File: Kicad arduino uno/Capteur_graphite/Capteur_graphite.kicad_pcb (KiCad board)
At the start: 2 copper layers, 68.6 x 53.3 mm, 25 parts, among them J1 Power, J2 Digital/PWM, J3 Analog, J4 Digital/PWM, U3 MCP41050, U4 LTC1050

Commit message: masse flottante à refaire
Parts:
- moved U3 31.6 mm to (112.4, 51.9)
- moved R5 2.00 mm to (148.4, 93.5)
- moved U7 2.00 mm to (164.5, 92.0)
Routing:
- net P13: track 68.2 -> 28.5 mm
- net Net-(U3-PB0): track 62.2 -> 32.7 mm
- net P11: track 52.9 -> 34.1 mm
- net P10: track 48.6 -> 35.4 mm
- net +5V: track 193.8 -> 205.7 mm
- net A0: track 13.3 -> 11.3 mm
- net Net-(C4-Pad1): track 25.4 -> 24.2 mm
- net Net-(U5-OUT): track 6.21 -> 5.62 mm
- net P2: track 23.3 -> 22.7 mm

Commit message: Save_avec_via
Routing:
- net GND: track 0.00 -> 19.4 mm, vias 0 -> 6
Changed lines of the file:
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@@
+	)
+	(segment
+		(start 119.5 96.5)
+		(end 124 92)
+		(width 0.5)
+		(layer "F.Cu")
+		(net 1)
+	)
+	(segment
+		(start 135 92)
+		(end 141 92)
+		(width 0.5)
+		(layer "F.Cu")
+		(net 1)
+	)
+	(segment
+		(start 131.5 57.5)
+		(end 138.5 57.5)
+		(width 0.5)
+		(layer "F.Cu")
+		(net 1)
+	)
+	(via
+		(at 131.5 57.5)
+		(size 2)
+		(drill 1)
+		(layers "F.Cu" "B.Cu")
+		(free yes)
+		(net 1)
+	)
+	(via
+		(at 124 92)
+		(size 2)
+		(drill 1)
+		(layers "F.Cu" "B.Cu")
+		(free yes)
+		(net 1)
+	)
+	(via
+		(at 135 92)
+		(size 2)
+		(drill 1)
+		(layers "F.Cu" "B.Cu")
+		(free yes)
+		(net 1)
+	)
+	(via
+		(at 138.5 57.5)
+		(size 2)
+		(drill 1)
+		(layers "F.Cu" "B.Cu")
+		(free yes)
+		(net 1)
+	)
+	(via
+		(at 141 92)
+		(size 2)
+		(drill 1)
+		(layers "F.Cu" "B.Cu")
+		(free yes)
+		(net 1)
+	)
+	(via
+		(at 119.5 96.5)
+		(size 2)
+		(drill 1)
+		(layers "F.Cu" "B.Cu")
+		(free yes)
+		(net 1)
 	)
 	(segment

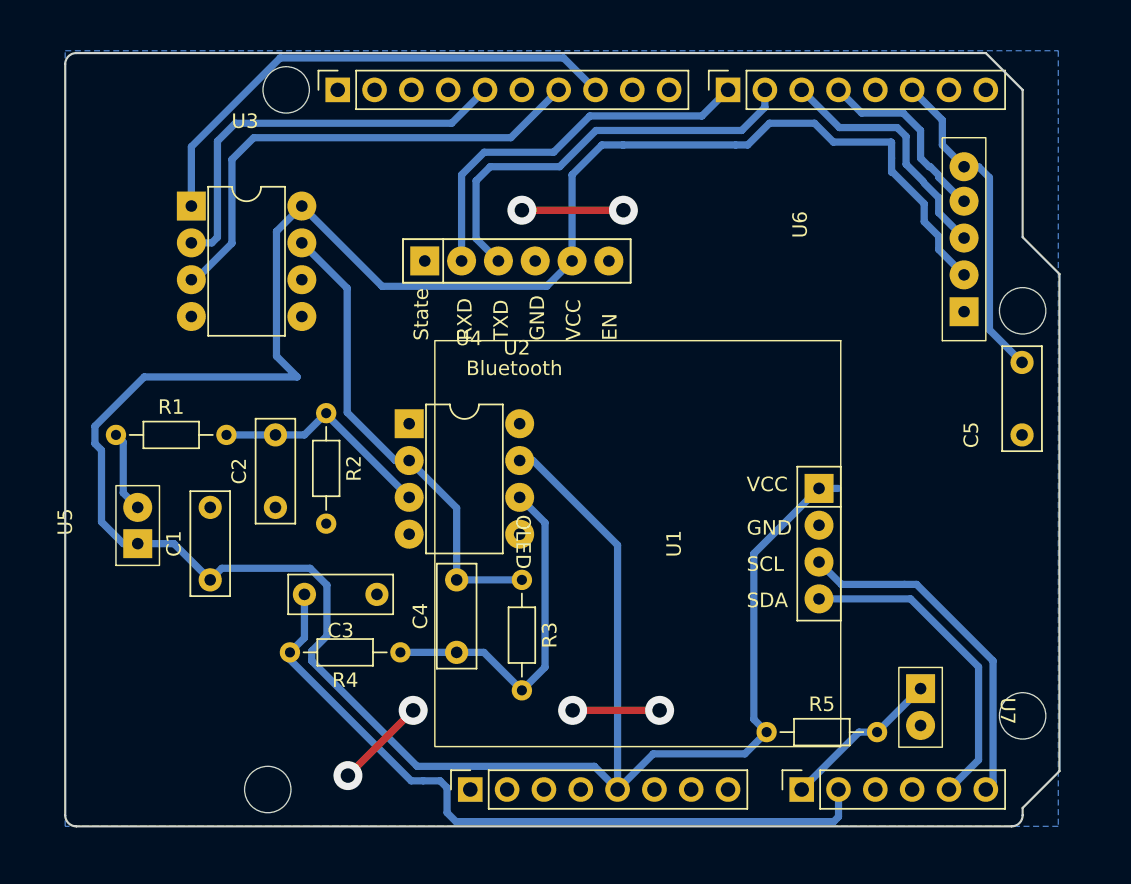
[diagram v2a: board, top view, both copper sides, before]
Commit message: Save_sans_via_mais_avec_modif_pin
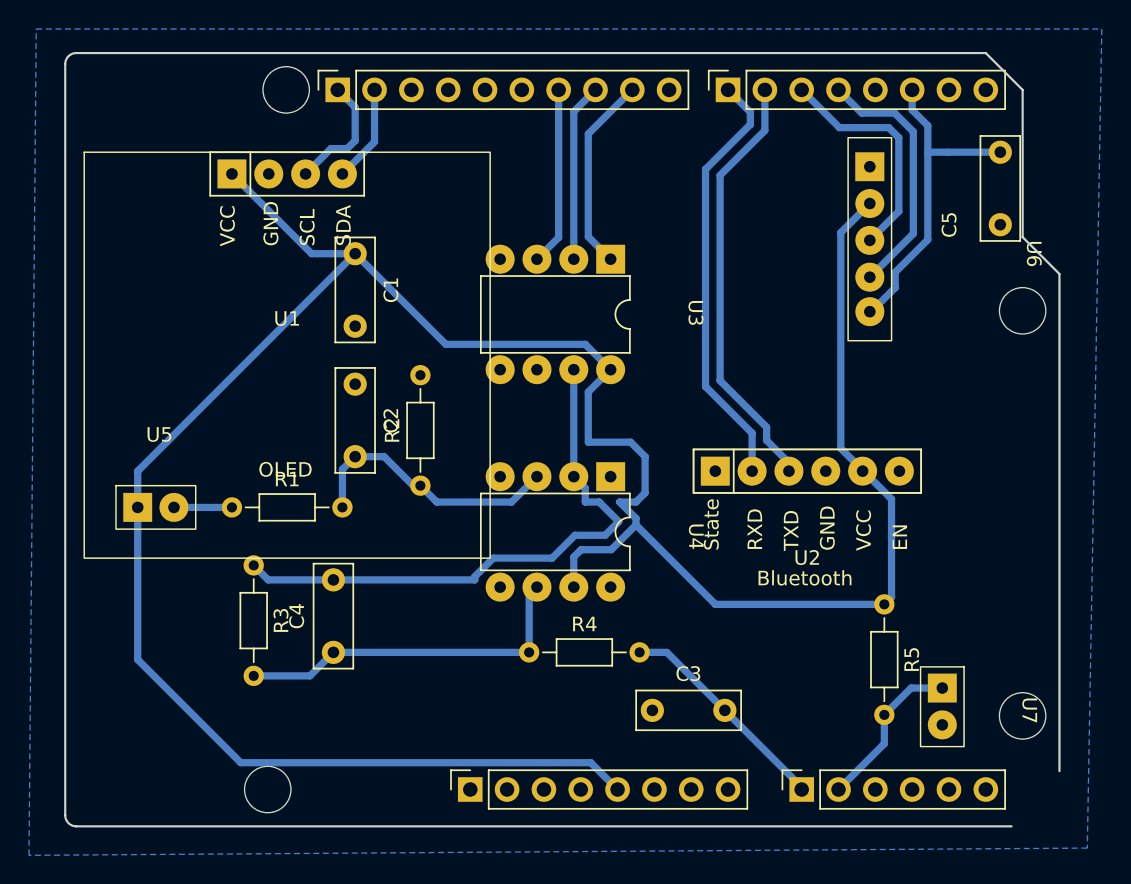
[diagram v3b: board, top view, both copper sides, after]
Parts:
- moved U1 44.7 mm to (115.3, 55.0), turned to 0 degrees
- moved U3 33.1 mm to (143.0, 64.6), turned to -90 degrees
- moved U2 24.7 mm to (151.2, 75.5)
- moved C1 24.6 mm to (120.0, 60.5), turned to -90 degrees
- moved C3 20.6 mm to (140.5, 92.0), turned to 0 degrees
- moved U4 20.1 mm to (143.0, 80.0), turned to -90 degrees
- moved R3 18.5 mm to (113.0, 82.0)
- moved C5 14.6 mm to (164.5, 58.5)
- moved R5 12.0 mm to (156.5, 84.7), turned to -90 degrees
- moved C2 10.1 mm to (120.0, 69.5), turned to -90 degrees
- moved R1 9.43 mm to (111.5, 78.0)
- moved R4 8.88 mm to (132.0, 88.0), turned to 0 degrees
- moved C4 8.50 mm to (118.5, 88.0)
- moved R2 8.20 mm to (124.5, 76.5), turned to 90 degrees
- moved U5 8.14 mm to (106.5, 73.5), turned to 0 degrees
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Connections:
- C3 pad 2: A1 -> A0
- J2 pad 5: P13 -> /13
- J2 pad 9: /*9 -> P9
- R4 pad 2: A1 -> A0
- R5 pad 2: A0 -> A1
- U3 pad 1: P10 -> P9
- U3 pad 2: P13 -> P10
- U7 pad 1: A0 -> A1
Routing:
- net A1: track 50.4 -> 11.2 mm
- net +5V: track 205.7 -> 176.6 mm
- net P13: track 28.5 -> 0.00 mm
- net P10: track 35.4 -> 12.3 mm
- net P11: track 34.1 -> 12.3 mm
- net GND: track 19.4 -> 0.00 mm, vias 6 -> 0
- net A4: track 22.3 -> 6.72 mm
- net A5: track 23.9 -> 8.37 mm
- net P9: track 0.00 -> 13.6 mm
- net Net-(U3-PB0): track 32.7 -> 39.7 mm
- net P4: track 13.0 -> 17.6 mm
- net A0: track 11.3 -> 15.2 mm
- net P7: track 26.7 -> 29.5 mm
- net Net-(C2-Pad2): track 15.7 -> 18.4 mm
- net Net-(U5-OUT): track 5.62 -> 4.00 mm
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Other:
- outline, holes or cut-outs redrawn
- board text removed: "${REFERENCE}"
- board text removed: "ICSP"

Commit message: sans_via_mais_bonne_modif_pin_(SCK_sur_la_13)
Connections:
- J2 pad 5: /13 -> P13
- J2 pad 8: P10 -> /*10
- U3 pad 2: P10 -> P13
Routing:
- net P13: track 0.00 -> 39.2 mm
- net P10: track 12.3 -> 0.00 mm
- net P11: track 12.3 -> 18.7 mm
- net P2: track 22.5 -> 24.0 mm
- net P9: track 13.6 -> 12.3 mm
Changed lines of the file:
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@@
 	(net 7 "/12")
 	(net 8 "/AREF")
-	(net 9 "/13")
+	(net 9 "P13")
 	(net 10 "/TX{slash}1")
 	(net 11 "/*3")
@@
 	(net 19 "unconnected-(U2-State-Pad1)")
 	(net 20 "unconnected-(U2-EN-Pad6)")
-	(net 21 "P10")
+	(net 21 "/*10")
 	(net 22 "P11")
 	(net 23 "Net-(U5-OUT)")
@@
 			(layers "*.Cu" "*.Mask")
 			(remove_unused_layers no)
-			(net 9 "/13")
+			(net 9 "P13")
 			(pinfunction "Pin_5")
 			(pintype "passive")
@@
 			(layers "*.Cu" "*.Mask")
 			(remove_unused_layers no)
-			(net 21 "P10")
+			(net 21 "/*10")
 			(pinfunction "Pin_8")
 			(pintype "passive")
@@
 		(tags "C Disc series Radial pin pitch 5.00mm  diameter 7mm width 2.5mm Capacitor")
 		(property "Reference" "C3"
-			(at 2.5 -2.5 360)
+			(at 2.5 -2.5 0)
 			(layer "F.SilkS")
 			(effects
@@
 		)
 		(property "Value" "C"
-			(at 2.5 2.5 360)
+			(at 2.5 2.5 0)
 			(layer "F.Fab")
 			(effects
@@
 		)
 		(fp_text user "${REFERENCE}"
-			(at 2.5 0 360)
+			(at 2.5 0 0)
 			(layer "F.Fab")
 			(effects
@@
 			(layers "*.Cu" "*.Mask")
 			(remove_unused_layers no)
-			(net 21 "P10")
+			(net 9 "P13")
 			(pinfunction "SCK")
 			(pintype "passive")
@@
 		(tags "Resistor Axial_DIN0204 series Axial Horizontal pin pitch 7.62mm 0.167W length 3.6mm diameter 1.6mm")
 		(property "Reference" "R4"
-			(at 3.81 -1.92 360)
+			(at 3.81 -1.92 0)
 			(layer "F.SilkS")
 			(effects
@@
 		)
 		(property "Value" "R"
-			(at 3.81 1.92 360)
+			(at 3.81 1.92 0)
 			(layer "F.Fab")
 			(effects
@@
 		)
 		(fp_text user "${REFERENCE}"
-			(at 3.81 0 360)
+			(at 3.81 0 0)
 			(layer "F.Fab")
 			(effects
@@
 		(at 115.31 55)
 		(property "Reference" "U1"
-			(at 0 10 360)
+			(at 0 10 0)
 			(layer "F.SilkS")
 			(effects
@@
 		)
 		(property "Value" "~"
-			(at 0 -2.5 360)
+			(at 0 -2.5 0)
 			(layer "F.Fab")
 			(effects
@@
 		)
 		(property "Footprint" "Librairie_d_empreinte:OLED"
-			(at 0 0 360)
+			(at 0 0 0)
 			(layer "F.Fab")
 			(hide yes)
@@
 		)
 		(property "Datasheet" ""
-			(at 0 0 360)
+			(at 0 0 0)
 			(layer "F.Fab")
 			(hide yes)
@@
 		)
 		(property "Description" ""
-			(at 0 0 360)
+			(at 0 0 0)
 			(layer "F.Fab")
 			(hide yes)
@@
 		(tags "Resistor Axial_DIN0204 series Axial Horizontal pin pitch 7.62mm 0.167W length 3.6mm diameter 1.6mm")
 		(property "Reference" "R1"
-			(at 3.81 -1.92 360)
+			(at 3.81 -1.92 0)
 			(layer "F.SilkS")
 			(effects
@@
 		)
 		(property "Value" "R"
-			(at 3.81 1.92 360)
+			(at 3.81 1.92 0)
 			(layer "F.Fab")
 			(effects
@@
 		)
 		(fp_text user "${REFERENCE}"
-			(at 3.81 0 360)
+			(at 3.81 0 0)
 			(layer "F.Fab")
 			(effects
@@
 		(layer "Edge.Cuts")
 	)
+	(gr_line
+		(start 168.58 96.19)
+		(end 165.278 100)
+		(stroke
+			(width 0.15)
+			(type solid)
+		)
+		(layer "Edge.Cuts")
+	)
 	(gr_arc
 		(start 100 47.422)
@@
 	)
 	(segment
+		(start 130.656 47.5)
+		(end 128.956 49.2)
+		(width 0.5)
+		(layer "B.Cu")
+		(net 9)
+	)
+	(segment
+		(start 140 51.5)
+		(end 140.7 50.8)
+		(width 0.5)
+		(layer "B.Cu")
+		(net 9)
+	)
+	(segment
+		(start 140 62.5)
+		(end 140 51.5)
+		(width 0.5)
+		(layer "B.Cu")
+		(net 9)
+	)
+	(segment
+		(start 142.318742 50.8)
+		(end 143.5 49.618742)
+		(width 0.5)
+		(layer "B.Cu")
+		(net 9)
+	)
+	(segment
+		(start 135.785787 63)
+		(end 139.5 63)
+		(width 0.5)
+		(layer "B.Cu")
+		(net 9)
+	)
+	(segment
+		(start 143.5 48)
+		(end 143 47.5)
+		(width 0.5)
+		(layer "B.Cu")
+		(net 9)
+	)
+	(segment
+		(start 135.08 60.88)
+		(end 135.08 62.294213)
+		(width 0.5)
+		(layer "B.Cu")
+		(net 9)
+	)
+	(segment
+		(start 135.08 62.294213)
+		(end 135.785787 63)
+		(width 0.5)
+		(layer "B.Cu")
+		(net 9)
+	)
+	(segment
+		(start 143.5 49.618742)
+		(end 143.5 48)
+		(width 0.5)
+		(layer "B.Cu")
+		(net 9)
+	)
+	(segment
+		(start 143 47.5)
+		(end 130.656 47.5)
+		(width 0.5)
+		(layer "B.Cu")
+		(net 9)
+	)
+	(segment
+		(start 140.7 50.8)
+		(end 142.318742 50.8)
+		(width 0.5)
+		(layer "B.Cu")
+		(net 9)
+	)
+	(segment
+		(start 139.5 63)
+		(end 140 62.5)
+		(width 0.5)
+		(layer "B.Cu")
+		(net 9)
+	)
+	(segment
 		(start 122 74.5)
 		(end 120 74.5)
@@
 	)
 	(segment
-		(start 135.08 50.696)
-		(end 135.08 60.88)
+		(start 137.414214 59.085786)
+		(end 134.334214 59.085786)
 		(width 0.5)
 		(layer "B.Cu")
-		(net 21)
+		(net 22)
 	)
 	(segment
-		(start 136.576 49.2)
-		(end 135.08 50.696)
+		(start 134.976 49.2)
+		(end 134.976 49.862742)
 		(width 0.5)
 		(layer "B.Cu")
-		(net 21)
+		(net 22)
 	)
 	(segment
-		(start 134.036 49.2)
-		(end 134.036 59.384)
+		(start 134.976 49.862742)
+		(end 135.913258 50.8)
+		(width 0.5)
+		(layer "B.Cu")
+		(net 22)
+	)
+	(segment
+		(start 137.218 50.8)
+		(end 138 51.582)
 		(width 0.5)
 		(layer "B.Cu")
@@
 	)
 	(segment
-		(start 134.036 59.384)
+		(start 134.334214 59.085786)
 		(end 132.54 60.88)
 		(width 0.5)
@@
 	)
 	(segment
+		(start 134.036 49.2)
+		(end 134.976 49.2)
+		(width 0.5)
+		(layer "B.Cu")
+		(net 22)
+	)
+	(segment
+		(start 135.913258 50.8)
+		(end 137.218 50.8)
+		(width 0.5)
+		(layer "B.Cu")
+		(net 22)
+	)
+	(segment
+		(start 138 58.5)
+		(end 137.414214 59.085786)
+		(width 0.5)
+		(layer "B.Cu")
+		(net 22)
+	)
+	(segment
+		(start 138 51.582)
+		(end 138 58.5)
+		(width 0.5)
+		(layer "B.Cu")
+		(net 22)
+	)
+	(segment
 		(start 107.5 78)
 		(end 111.5 78)
@@
 	)
 	(segment
-		(start 157.25 62.844874)
-		(end 157.25 61.784214)
+		(start 159.5 51.671572)
+		(end 164 51.671572)
 		(width 0.5)
 		(layer "B.Cu")
@@
 	)
 	(segment
-		(start 160.92 53.5)
-		(end 159.5 53.5)
+		(start 157.25 62.844874)
+		(end 157.25 61.784214)
 		(width 0.5)
 		(layer "B.Cu")
@@
 	)
 	(segment
-		(start 164.5 53.5)
-		(end 160.92 53.5)
+		(start 164 51.671572)
+		(end 164.5 52.171572)
 		(width 0.5)
 		(layer "B.Cu")
@@
 	)
 	(segment
+		(start 164.5 52.171572)
+		(end 164.5 53.5)
+		(width 0.5)
+		(layer "B.Cu")
+		(net 25)
+	)
+	(segment
 		(start 157.25 61.784214)
 		(end 159.5 59.534214)
@@
 	)
 	(segment
-		(start 139.116 49.2)
-		(end 136.08 52.236)
+		(start 139 49.316)
+		(end 139 59.5)
 		(width 0.5)
 		(layer "B.Cu")
@@
 	)
 	(segment
-		(start 136.08 59.34)
-		(end 137.62 60.88)
+		(start 139.116 49.2)
+		(end 139 49.316)
 		(width 0.5)
 		(layer "B.Cu")
@@
 	)
 	(segment
-		(start 136.08 52.236)
-		(end 136.08 59.34)
+		(start 139 59.5)
+		(end 137.62 60.88)
 		(width 0.5)
 		(layer "B.Cu")
@@
 		(polygon
 			(pts
-				(xy 98 45) (xy 171.5 45) (xy 170.5 101.5) (xy 97.5 102)
+				(xy 100 46.5) (xy 168.5 46.5) (xy 168.5 100) (xy 100 100)
 			)
 		)
